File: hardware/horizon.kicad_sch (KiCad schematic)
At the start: 8 parts, among them J1 USB_C_Receptacle_PowerOnly_6P, SW1 SW_Push, U1 ESP32-S3, U2 NCP1529A

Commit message: Working on PD and QSPI
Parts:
- added BT1: Battery, symbol Device:Battery
- added R4, R5: 5.1k, symbol Device:R
- added U3: W25Q128JVS, Package_SO:SOIC-8_5.3x5.3mm_P1.27mm, symbol Memory_Flash:W25Q128JVS
- added U4: BQ24074RGT, Package_DFN_QFN:VQFN-16-1EP_3x3mm_P0.5mm_EP1.6x1.6mm, symbol Battery_Management:BQ24074RGT
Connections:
- net 5V GND is gone; now on net GND: J1.SH (SHIELD)
- net 3.3V: now also U3.8 (VCC)
- net GND: now also BT1.2 (-), R4.2, R5.2, U3.4 (GND), U4.17 (VSS), U4.4 (~{CE}), U4.6 (EN1), U4.8 (VSS)
- net at J1.A5 (CC1): now also R4.1
- net at J1.B5 (CC2): now also R5.1
- net QSPI_HOLD: now reaches U1.30 (SPIHD)
- net QSPI_HOLD: now also U3.7 (~{HOLD}/~{RESET}/IO_{3})
- net QSPI_WP: now reaches U1.31 (SPIWP)
- net QSPI_WP: now also U3.3 (~{WP}/IO_{2})
- net QSPI_CS: now reaches U1.32 (SPICS0)
- net QSPI_CS: now also U3.1 (~{CS})
- net QSPI_CLK: now reaches U1.33 (SPICLK)
- net QSPI_CLK: now also U3.6 (CLK)
- net QSPI_D0: now reaches U1.34 (SPIQ)
- net QSPI_D0: now also U3.2 (DO/IO_{1})
- net QSPI_D1: now reaches U1.35 (SPID)
- net QSPI_D1: now also U3.5 (DI/IO_{0})
- net SYS: now reaches U2.1 (EN), U2.4 (VIN)
- net SYS: now also U4.10 (OUT), U4.11 (OUT)
- net 5V renamed USB_5V
- net USB_5V: now also U4.13 (IN), U4.5 (EN2)
- new net: BT1.1 (+), U4.2 (BAT), U4.3 (BAT)

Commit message: Working on schematic
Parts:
- added J2: Conn_01x08_Socket, symbol Connector:Conn_01x08_Socket
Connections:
- net SPI_BUSY: now reaches U1.12 (GPIO7)
- net SPI_BUSY: now also J2.1 (Pin_1)
- net SPI_RESET: now reaches U1.13 (GPIO8)
- net SPI_RESET: now also J2.2 (Pin_2)
- net SPI_DC: now reaches U1.14 (GPIO9)
- net SPI_DC: now also J2.3 (Pin_3)
- net SPI_CS0: now reaches U1.15 (GPIO10)
- net SPI_CS0: now also J2.4 (Pin_4)
- net SPI_MOSI: now reaches U1.16 (GPIO11)
- net SPI_MOSI: now also J2.5 (Pin_5)
- net SPI_CLK: now reaches U1.17 (GPIO12)
- net SPI_CLK: now also J2.6 (Pin_6)
- net SPI_MISO: now reaches U1.18 (GPIO13)
- net SPI_MISO: now also J2.7 (Pin_7)
- net USB_D-: now reaches U1.25 (GPIO19/USB_D-)
- net USB_D+: now reaches U1.26 (GPIO20/USB_D+)
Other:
- note added: "For programming"
- note added: "Todo: Find docs and put proper pinout from driver board"

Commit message: Finished schematic draft
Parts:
- removed J1: USB_C_Receptacle_PowerOnly_6P, symbol Connector:USB_C_Receptacle_PowerOnly_6P
- removed J2: Conn_01x08_Socket, symbol Connector:Conn_01x08_Socket
- added C1, C2, C4: 100nF, symbol Device:C
- added C3: 10µF, symbol Device:C
- added C5: 22µF, symbol Device:C
- added C6, C7: 22pF, symbol Device:C
- added J1: Conn_01x14_Socket, symbol Connector:Conn_01x14_Socket
- added J3: USB_C_Receptacle_USB2.0_14P, symbol Connector:USB_C_Receptacle_USB2.0_14P
- added Status: LED_RGB, symbol Device:LED_RGB
- added Y1: CDX-1293, symbol Device:Crystal
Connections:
- net 3.3V: now also C1.1, C2.1, C4.1, C5.1
- net GND: now also C1.2, C2.2, C3.2, C4.2, C5.2, C6.2, C7.2, J1.1 (Pin_1), J1.10 (Pin_10), J1.8 (Pin_8), J3.A1 (GND), J3.A12 (GND), J3.B1 (GND), J3.B12 (GND), J3.SH (SHIELD), Status.1 (RK), Status.2 (GK), Status.3 (BK)
- net SPI_CLK: now also J1.5 (Pin_5)
- net SPI_CS0: now also J1.4 (Pin_4)
- net SPI_MISO: now also J1.6 (Pin_6)
- net SPI_MOSI: now also J1.7 (Pin_7)
- net SPI_RESET: now also J1.3 (Pin_3)
- net SYS: now also C3.1, J1.12 (Pin_12), J1.13 (Pin_13), J1.14 (Pin_14)
- net USB_5V: now also J3.A4 (VBUS), J3.A9 (VBUS), J3.B4 (VBUS), J3.B9 (VBUS)
- net USB_D+: now also J3.A6 (D+), J3.B6 (D+)
- net USB_D-: now also J3.A7 (D-), J3.B7 (D-)
- net at R5.1: now also J3.B5 (CC2)
- net at R4.1: now also J3.A5 (CC1)
- net SPI_HOSTHRDY: now reaches U1.19 (GPIO14)
- net SPI_HOSTHRDY: now also J1.2 (Pin_2)
- net at U1.21 (XTAL_32K_P): now also C6.1, Y1.2
- net at U1.22 (XTAL_32K_N): now also C7.1, Y1.1
- net at U1.40 (GPIO35): now also Status.4 (BA)
- net at U1.41 (GPIO36): now also Status.5 (GA)
- net at U1.42 (GPIO37): now also Status.6 (RA)
- net SPI_BUSY: no longer names the net of U1.12 (GPIO7)
- net SPI_DC renamed SPI_POWERCTRL
- net SPI_POWERCTRL: now also J1.9 (Pin_9)
- no-connect marks 0 -> 1
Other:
- note removed: "For programming"
- note removed: "Todo: Find docs and put proper pinout from driver board"

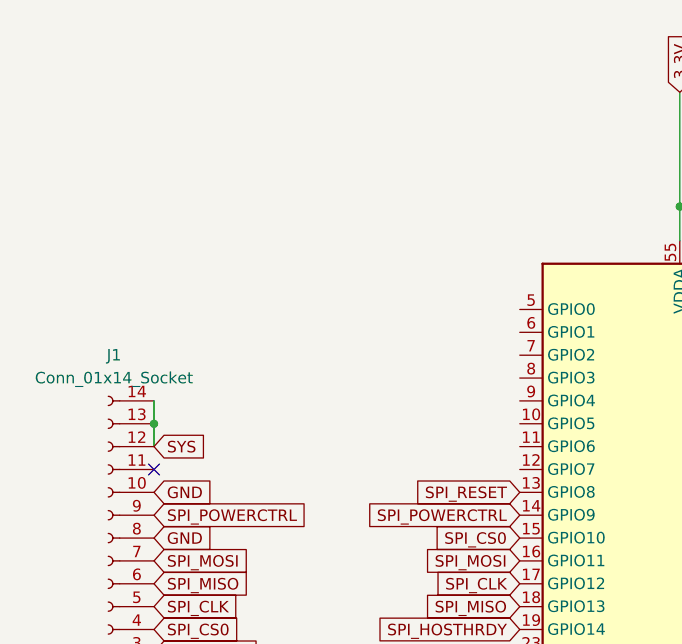
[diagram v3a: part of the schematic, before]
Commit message: Added touch I2C and working on adding driver for LVGL
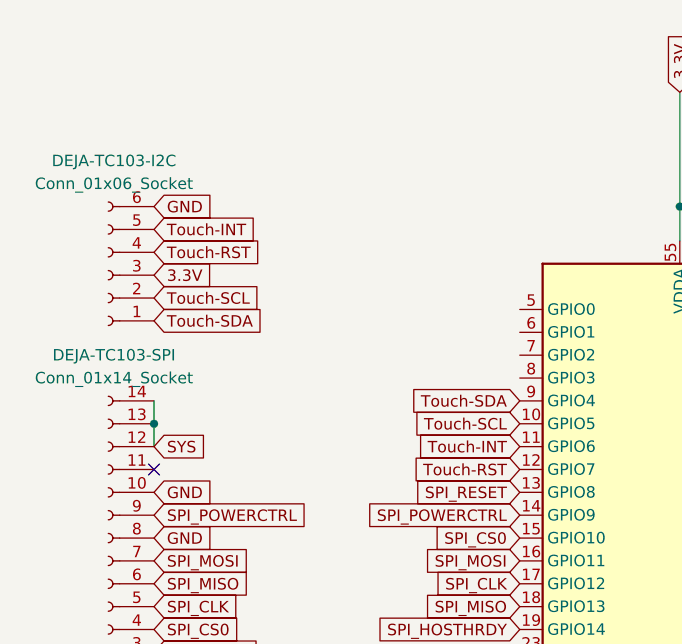
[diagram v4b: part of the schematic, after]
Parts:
- added DEJA-TC103-I2C: Conn_01x06_Socket, symbol Connector:Conn_01x06_Socket
- renumbered J1 to DEJA-TC103-SPI
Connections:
- net 3.3V: now also DEJA-TC103-I2C.3 (Pin_3)
- net GND: now also DEJA-TC103-I2C.6 (Pin_6)
- net Touch-SCL: now reaches U1.10 (GPIO5)
- net Touch-SCL: now also DEJA-TC103-I2C.2 (Pin_2)
- net Touch-INT: now reaches U1.11 (GPIO6)
- net Touch-INT: now also DEJA-TC103-I2C.5 (Pin_5)
- net Touch-RST: now reaches U1.12 (GPIO7)
- net Touch-RST: now also DEJA-TC103-I2C.4 (Pin_4)
- net Touch-SDA: now reaches U1.9 (GPIO4)
- net Touch-SDA: now also DEJA-TC103-I2C.1 (Pin_1)

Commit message: Finalising schematic
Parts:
- added R10, R9: 10kΩ, symbol Device:R
- added R11, R8: 18kΩ, symbol Device:R
- added R6: 2kΩ, symbol Device:R
- added R7: 1.8kΩ, symbol Device:R
- added TH1: Thermistor_NTC, symbol Device:Thermistor_NTC
- renumbered DEJA-TC103-I2C to DEJA-TC103-I2C1, DEJA-TC103-SPI to DEJA-TC103-SPI1, Status to Status1
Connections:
- net GND: now also R11.1, R6.1, R7.2, R8.1, TH1.2
- net at U4.1 (TS): now also TH1.1
- net at U4.12 (ILIM): now also R6.2
- net at U4.14 (TMR): now also R11.2
- net at U4.15 (ITERM): now also R8.2
- net at U4.16 (ISET): now also R7.1
- net PGOOD: now reaches U4.7 (~{PGOOD})
- net PGOOD: now also U1.38 (GPIO33), R10.1
- net CHG: now reaches U4.9 (~{CHG})
- net CHG: now also U1.39 (GPIO34), R9.1
- net 3.3V renamed +3.3V
- net +3.3V: now also R10.2, R9.2
- net SYS renamed +5V
- net USB_5V: no longer names the net of J3.A4 (VBUS), J3.A9 (VBUS), J3.B4 (VBUS), J3.B9 (VBUS), U4.13 (IN), U4.5 (EN2)
- no-connect marks 1 -> 23
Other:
- note added: "need footprint"
- moved on the sheet: C7

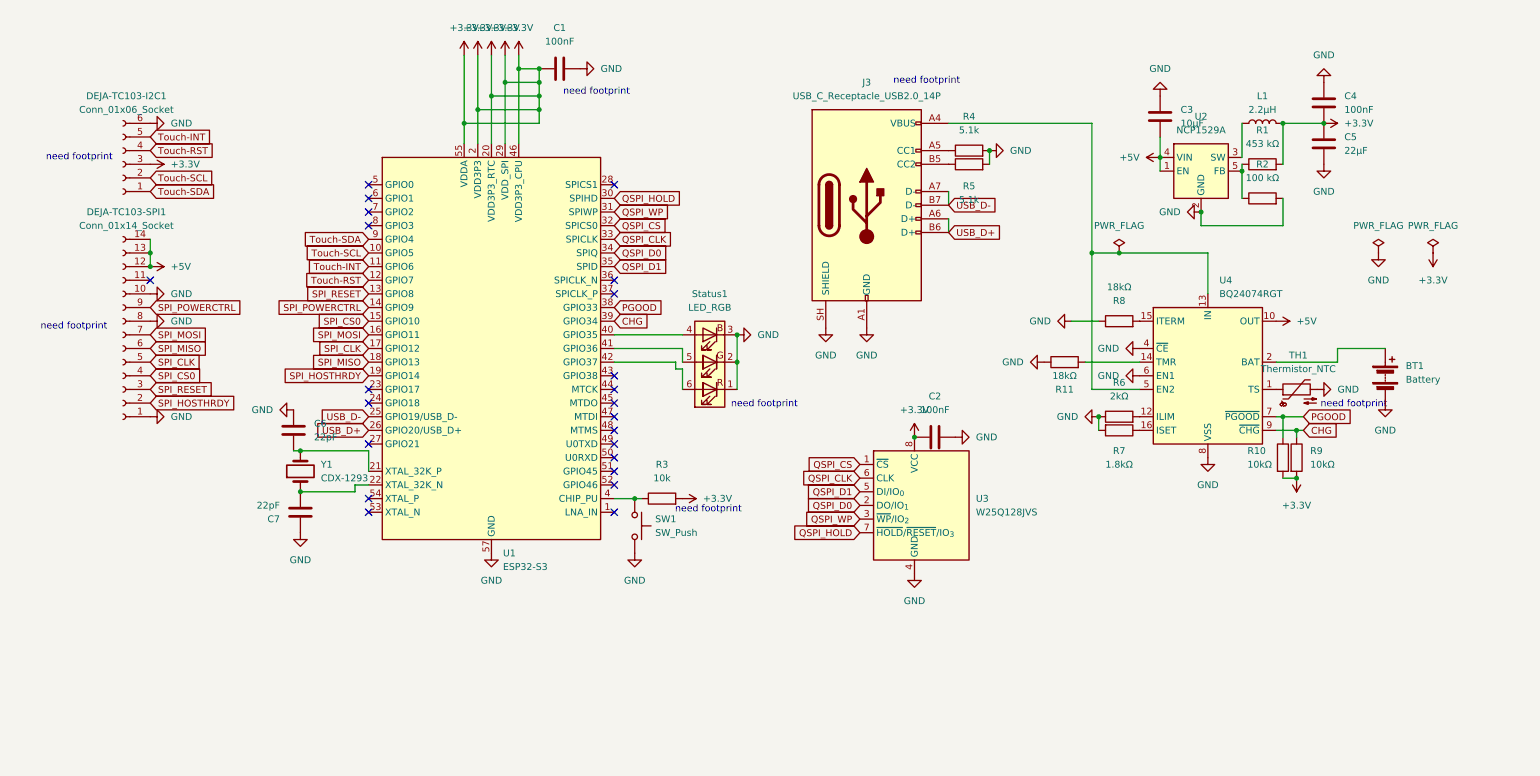
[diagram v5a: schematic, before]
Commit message: Finished schematic and began work on PCB
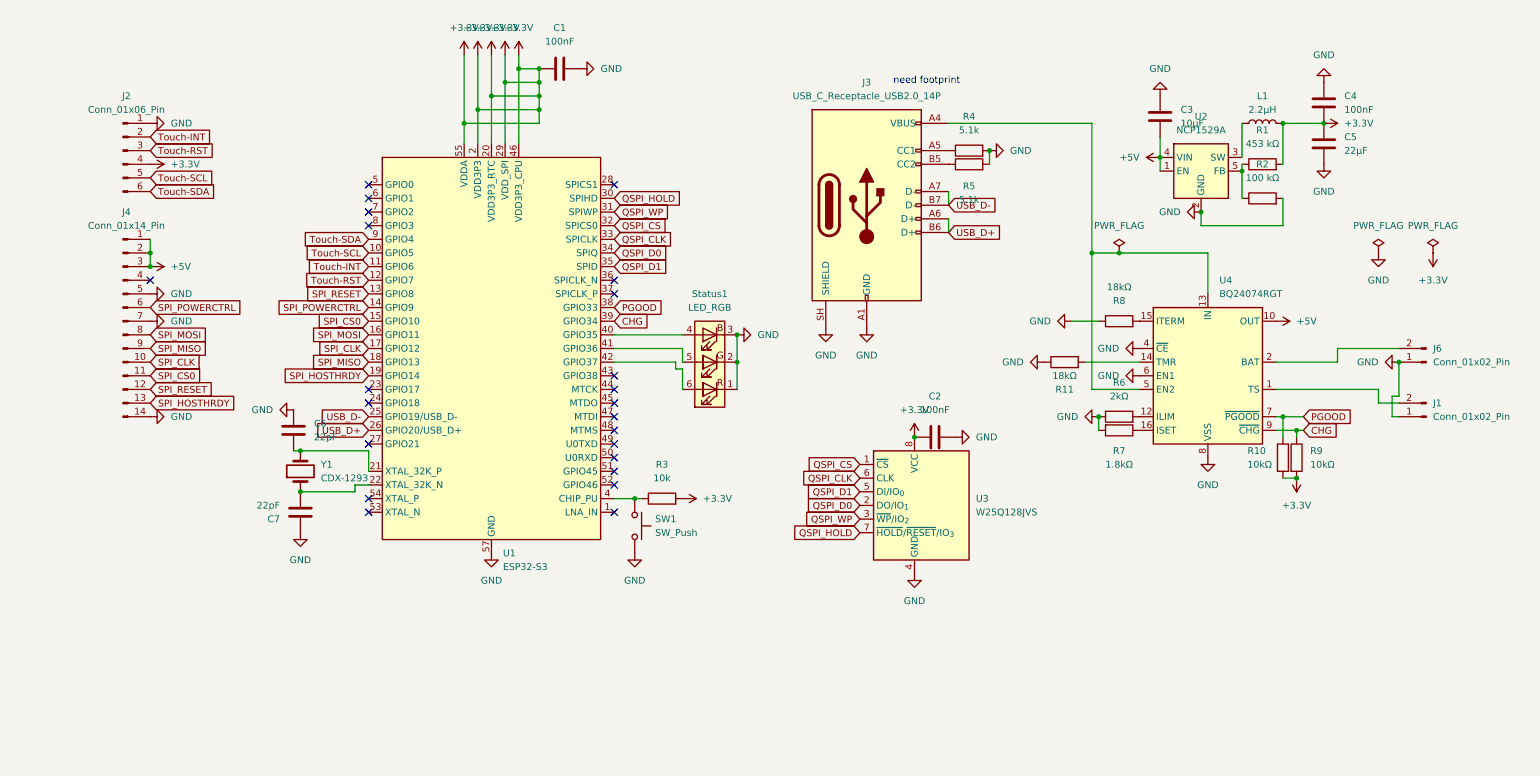
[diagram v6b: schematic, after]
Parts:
- removed BT1: Battery, symbol Device:Battery
- removed DEJA-TC103-I2C1: Conn_01x06_Socket, symbol Connector:Conn_01x06_Socket
- removed DEJA-TC103-SPI1: Conn_01x14_Socket, symbol Connector:Conn_01x14_Socket
- removed TH1: Thermistor_NTC, symbol Device:Thermistor_NTC
- added J1, J6: Conn_01x02_Pin, Connector_JST:JST_PH_S2B-PH-K_1x02_P2.00mm_Horizontal, symbol Connector:Conn_01x02_Pin
- added J2: Conn_01x06_Pin, Connector_PinHeader_2.54mm:PinHeader_1x06_P2.54mm_Horizontal, symbol Connector:Conn_01x06_Pin
- added J4: Conn_01x14_Pin, Connector_PinHeader_2.54mm:PinHeader_1x14_P2.54mm_Horizontal, symbol Connector:Conn_01x14_Pin
- C1, C2, C3, C4, C5, C6, C7: footprint (none) -> Capacitor_SMD:C_0201_0603Metric
- J3: footprint (none) -> Connector_USB:USB_C_Receptacle_HRO_TYPE-C-31-M-12
- L1: footprint (none) -> Inductor_SMD:L_Bourns_SDR0604
- R1, R10, R11, R2, R3, R4, R5, R6, R7, R8, R9: footprint (none) -> Resistor_SMD:R_0603_1608Metric
- SW1: footprint (none) -> Button_Switch_THT:SW_PUSH_6mm
- Status1: footprint (none) -> LED_SMD:LED_RGB_5050-6
- Y1: footprint (none) -> Crystal:Crystal_SMD_3215-2Pin_3.2x1.5mm
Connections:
- net +3.3V: now also J2.4 (Pin_4)
- net +5V: now also J4.1 (Pin_1), J4.2 (Pin_2), J4.3 (Pin_3)
- net GND: now also J1.1 (Pin_1), J2.1 (Pin_1), J4.14 (Pin_14), J4.5 (Pin_5), J4.7 (Pin_7), J6.1 (Pin_1)
- net SPI_CLK: now also J4.10 (Pin_10)
- net SPI_CS0: now also J4.11 (Pin_11)
- net SPI_HOSTHRDY: now also J4.13 (Pin_13)
- net SPI_MISO: now also J4.9 (Pin_9)
- net SPI_MOSI: now also J4.8 (Pin_8)
- net SPI_POWERCTRL: now also J4.6 (Pin_6)
- net SPI_RESET: now also J4.12 (Pin_12)
- net Touch-INT: now also J2.2 (Pin_2)
- net Touch-RST: now also J2.3 (Pin_3)
- net Touch-SCL: now also J2.5 (Pin_5)
- net Touch-SDA: now also J2.6 (Pin_6)
- net at U4.1 (TS): now also J1.2 (Pin_2)
- net at U4.2 (BAT), U4.3 (BAT): now also J6.2 (Pin_2)

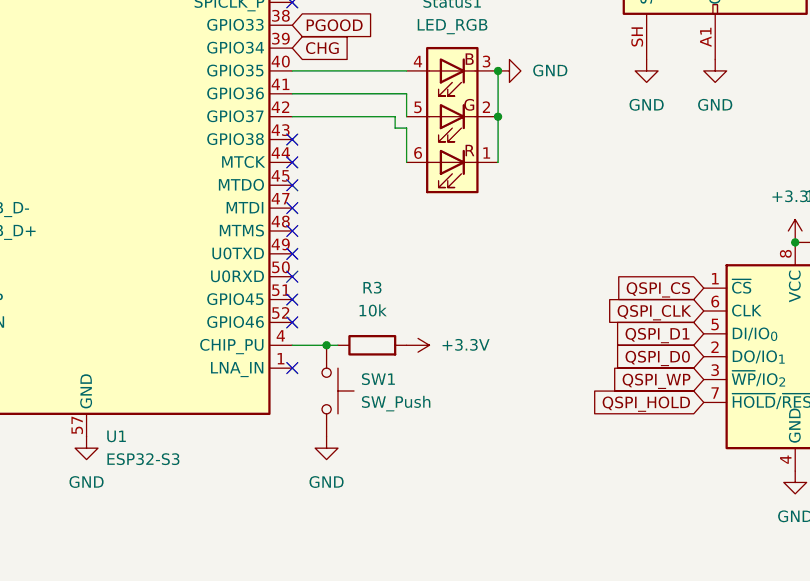
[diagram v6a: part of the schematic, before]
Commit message: added antenna
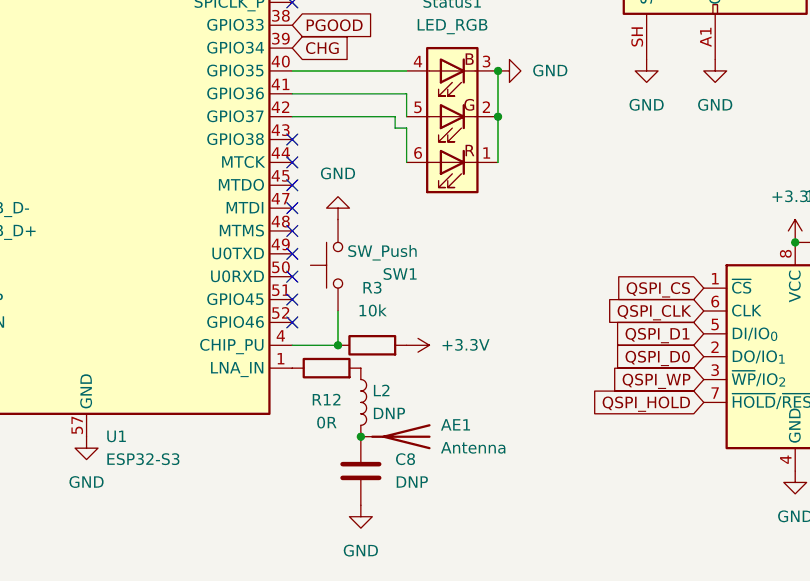
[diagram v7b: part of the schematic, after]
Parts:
- added AE1: Antenna, symbol Device:Antenna
- added C8: DNP, Capacitor_SMD:C_0201_0603Metric, symbol Device:C
- added L2: DNP, Inductor_SMD:L_Bourns_SDR0604, symbol Device:L
- added R12: 0R, Resistor_SMD:R_0603_1608Metric, symbol Device:R
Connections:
- net GND: now also C8.1
- net at U1.1 (LNA_IN): now also R12.1
- new net: L2.1, R12.2
- new net: AE1.1 (A), C8.2, L2.2
- no-connect marks 23 -> 22
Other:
- moved on the sheet: SW1

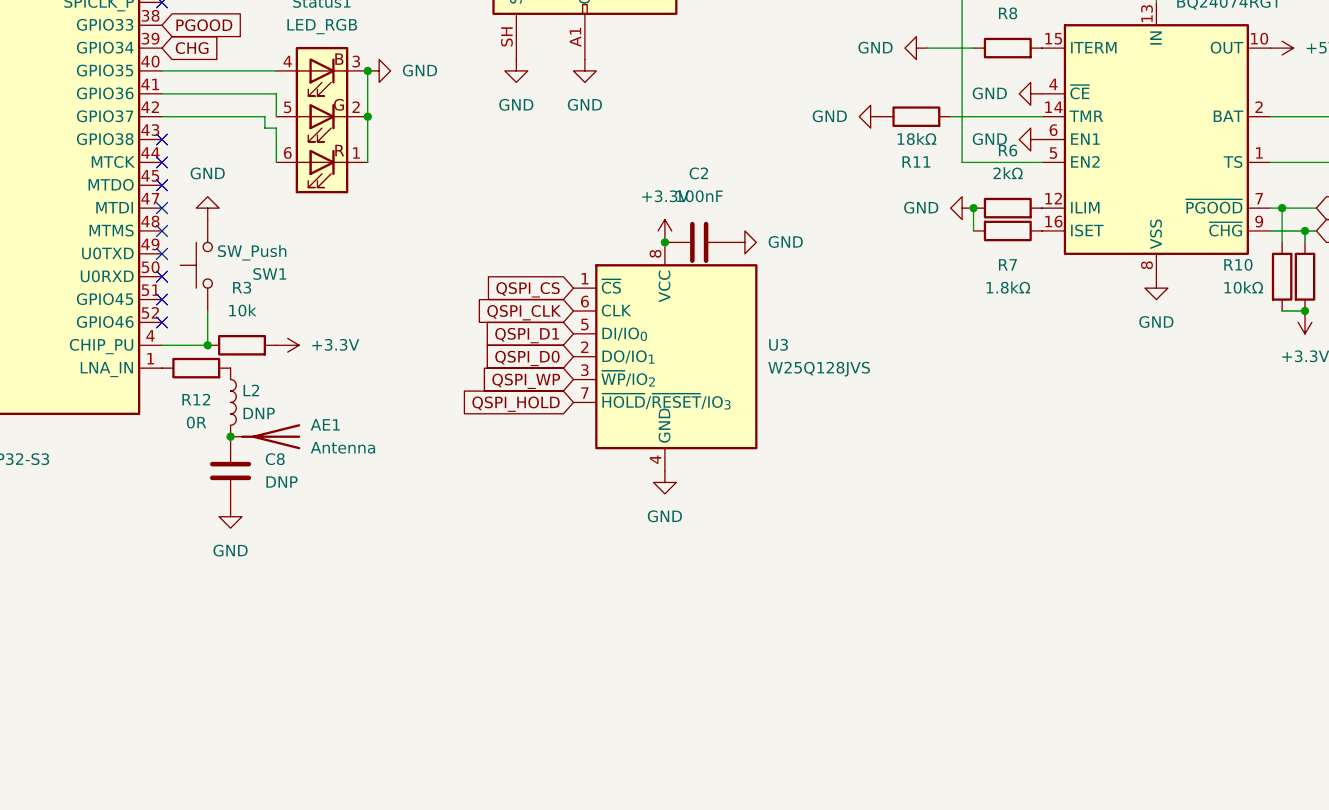
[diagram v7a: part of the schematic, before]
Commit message: Finished prototype pcb
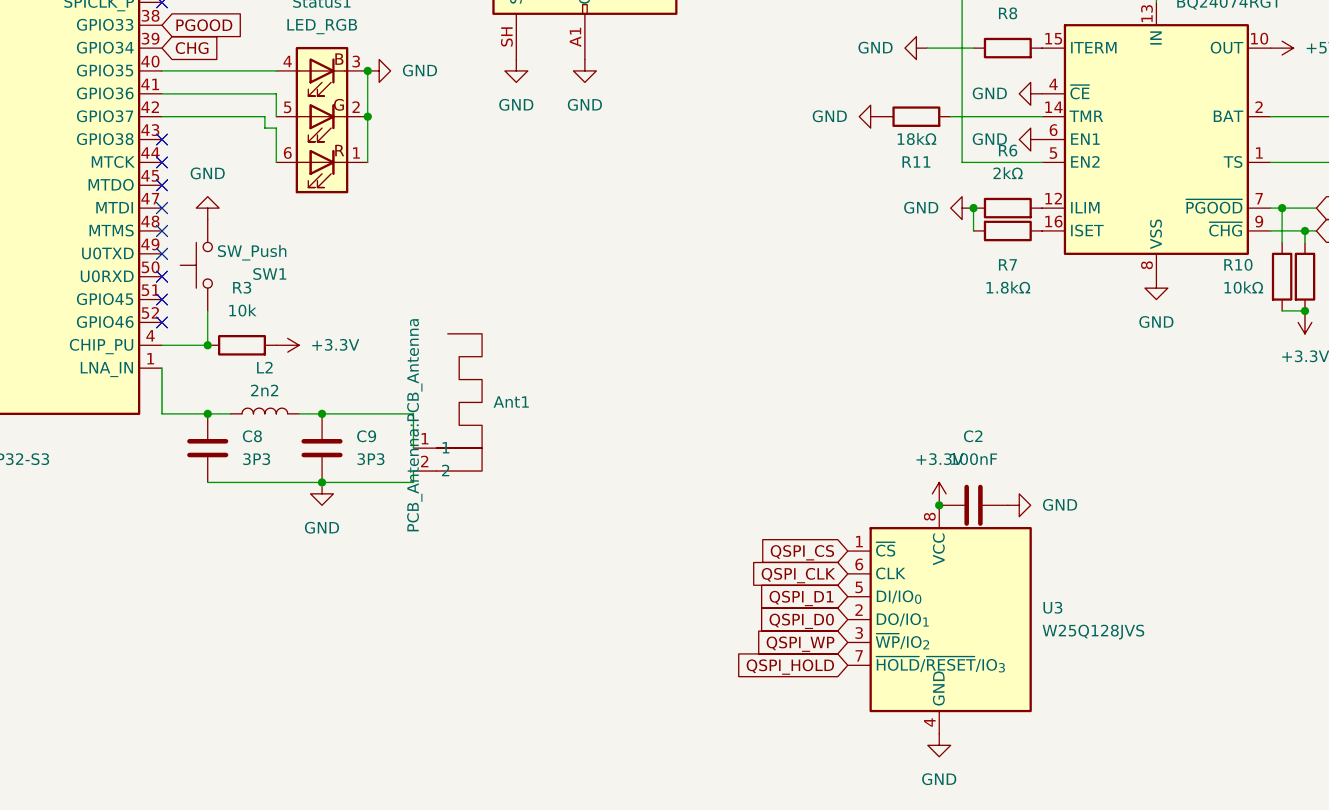
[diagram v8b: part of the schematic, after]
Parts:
- removed AE1: Antenna, symbol Device:Antenna
- removed R12: 0R, Resistor_SMD:R_0603_1608Metric, symbol Device:R
- added Ant1: PCB_Antenna:PCB_Antenna, PCB_Antenna:PCB_Antenna, symbol PCB_Antenna:PCB_Antenna
- added C9: 3P3, Capacitor_SMD:C_0201_0603Metric, symbol Device:C
- C8: value DNP -> 3P3
- L2: value DNP -> 2n2
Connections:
- net GND: now also C8.2, Ant1.2, C9.2; no longer C8.1
- net at U1.1 (LNA_IN): now also C8.1, L2.1
- net at L2.2: now also Ant1.1, C9.1; no longer C8.2
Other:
- moved on the sheet: C2, U3
